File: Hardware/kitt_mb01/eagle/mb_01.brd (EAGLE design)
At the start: 160 x 100 mm, 120 parts, among them IC2.00 BQ24266RGET, IC3.01 LSM9DS1, U1.01 RT8293A, U6.01 TPS61032RSARPSDO-G16, U7.01 SI1922EDH, U7.03 SI1922EDH, U7.2 SI1922EDH, X2.01 S2B-PH-K-S(LF)(SN), X7.02 ARDUINO_UNO, X7.03 CON_HEADER_1X02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

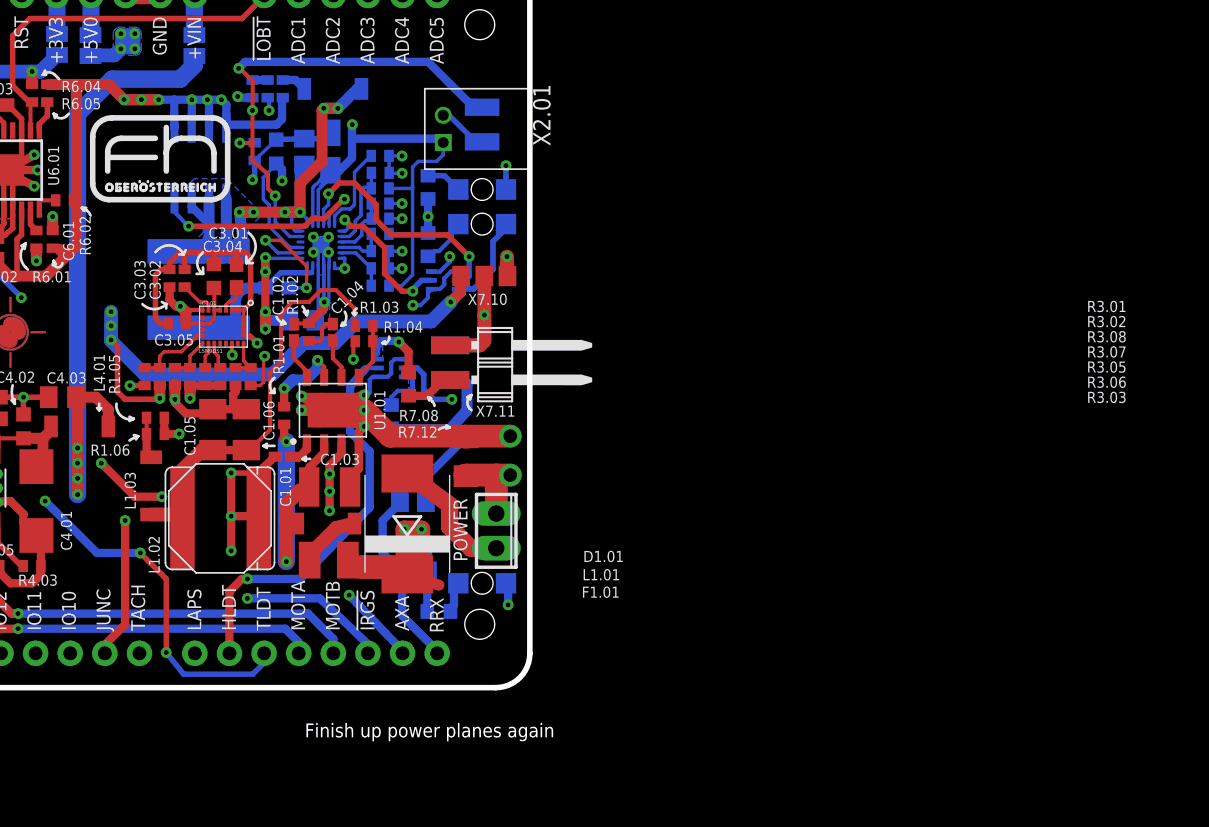
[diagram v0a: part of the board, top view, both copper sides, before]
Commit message: snapshot of mb01 board layout : finishing touches edition -> finished all placement, signal routing and component label silkscreen -> next up is maximization of power routes at layer 2 and -> ground pours on top and bottom with sufficient ground stitching
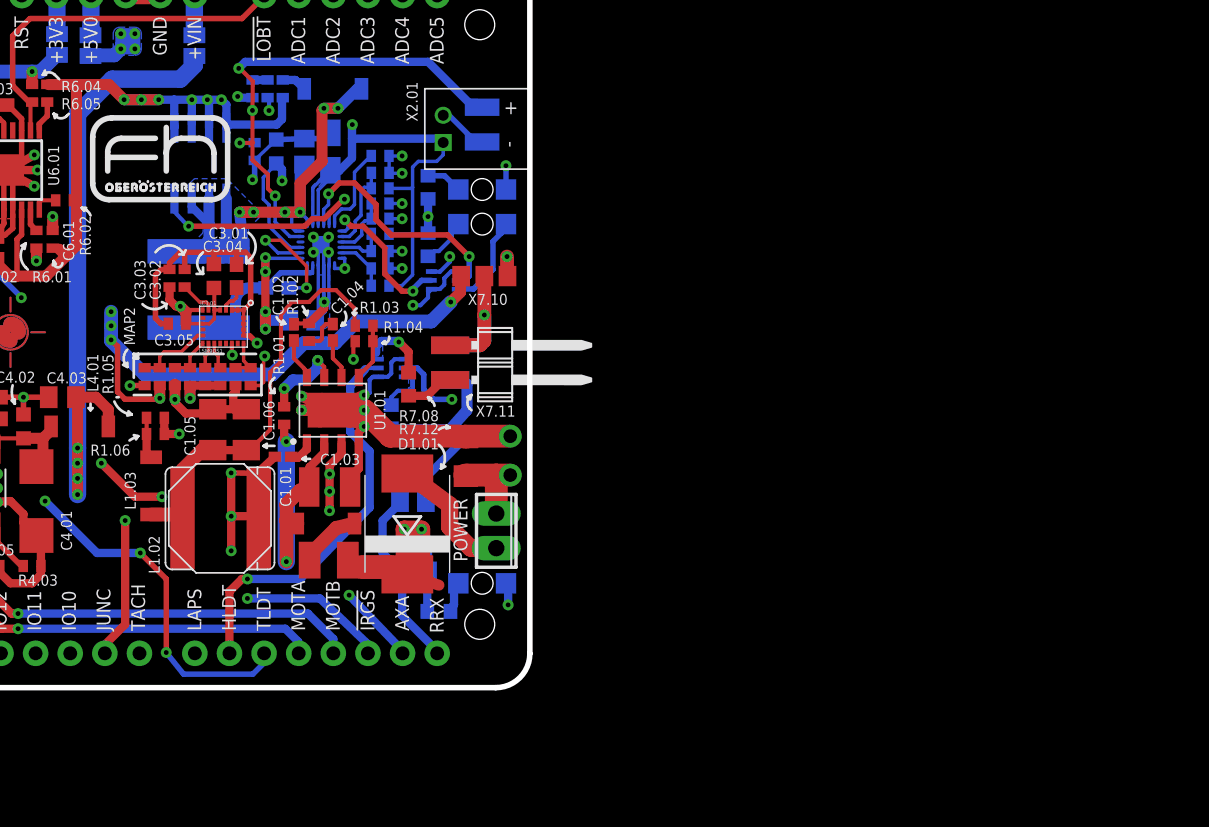
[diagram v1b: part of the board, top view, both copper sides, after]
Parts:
- renumbered IC2.00 to IC2.0, R7,01 to R7.16, R7,02 to R7.13, R7,04 to R7.14, R7,05 to R7.15
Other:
- board text added: "EXT.NTC"
- board text added: "MAP1"
- board text added: "MAP2"
- board text added: "TOP"
- board text removed: "<-- Rail Power Leads"
- board text removed: "EXT.PTC"
- board text removed: "Finish up power planes again"
- board text removed: "Motor Leads -->"
- board text removed: "SPEEDBOARD --> LAPDETECTOR -->"

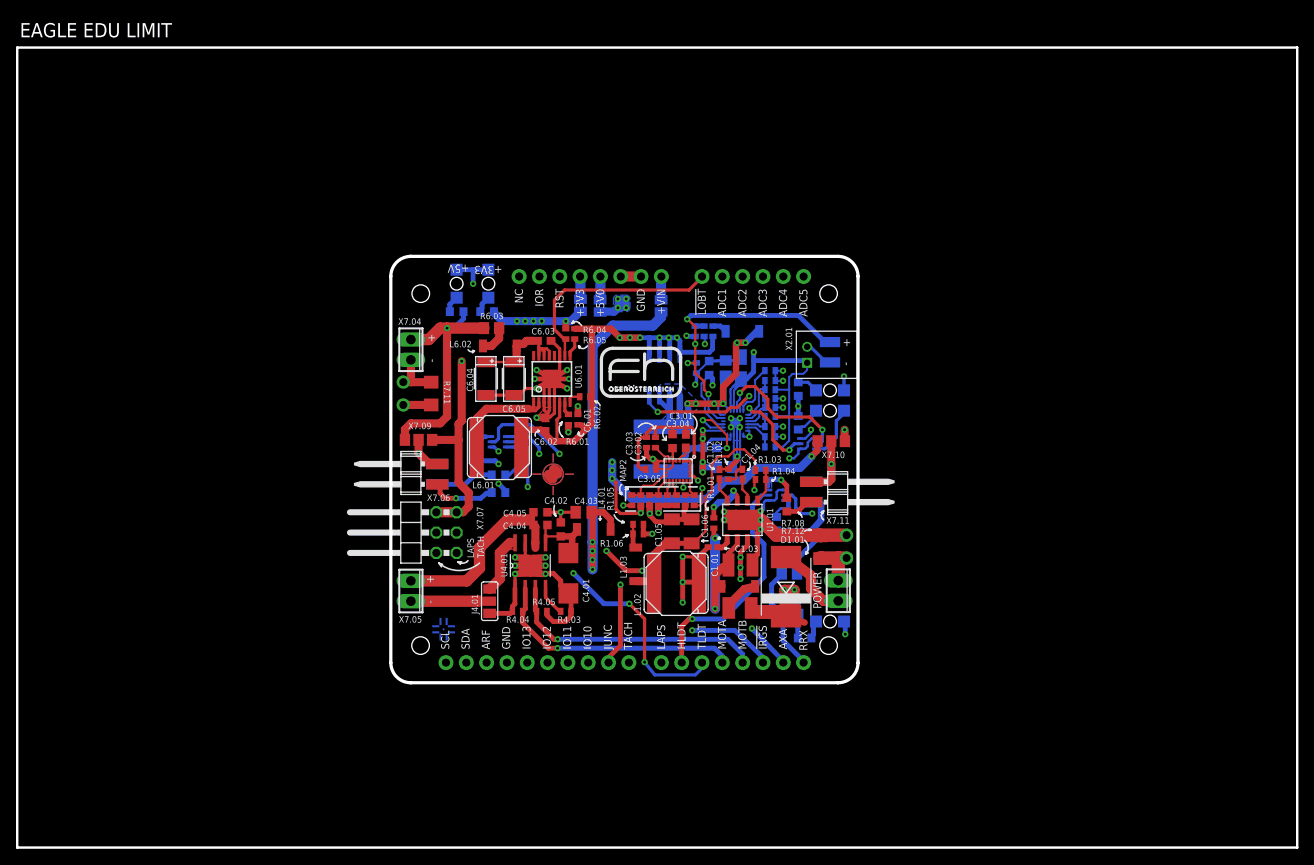
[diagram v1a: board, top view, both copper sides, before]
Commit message: snapshot of mb01 board layout -> where is the 3V3 supply again? -> there is none. will add optional LDO regulator which is on the BOM
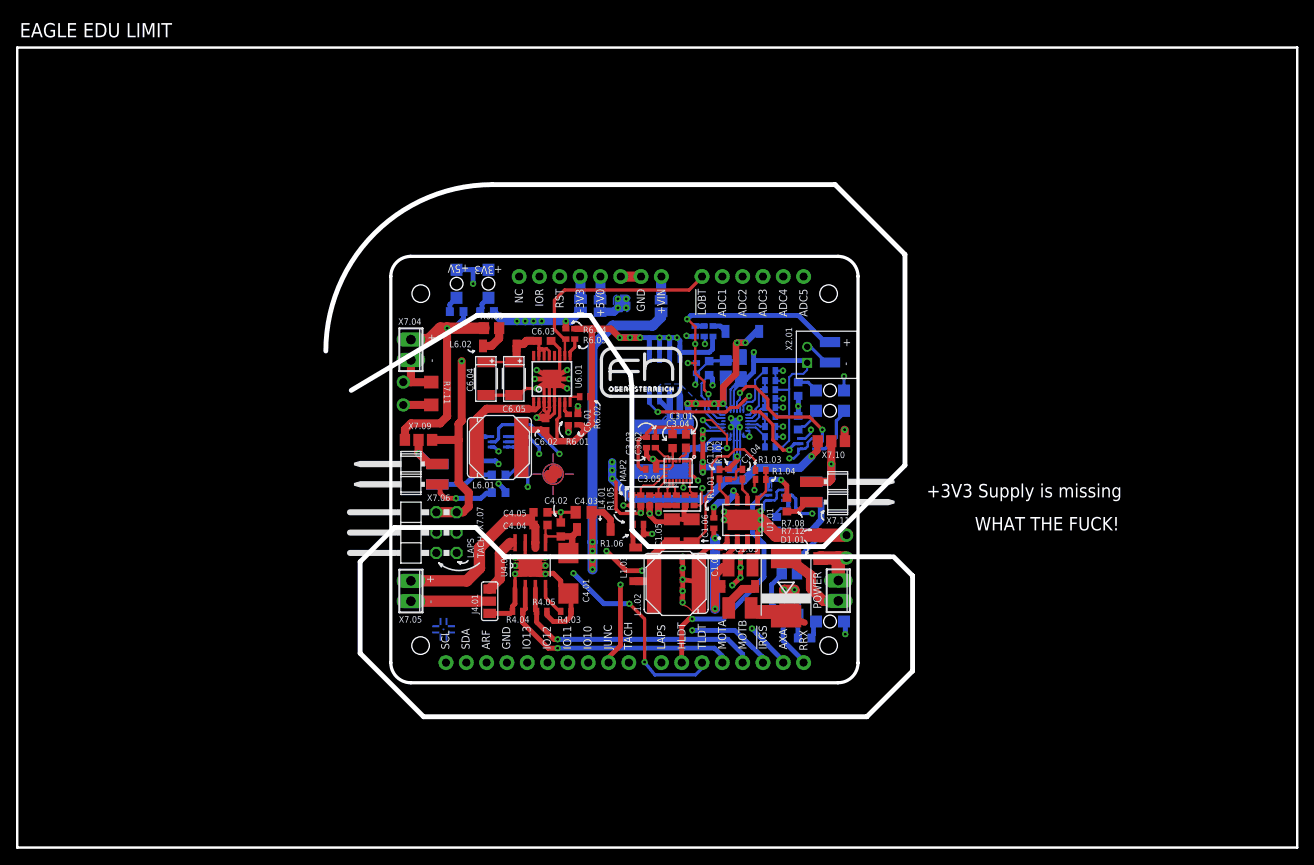
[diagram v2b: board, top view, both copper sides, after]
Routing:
- net N$88: track 17.5 -> 18.7 mm, vias 6 -> 9
- added copper zone on layer 1, net N$88
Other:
- outline, holes or cut-outs redrawn
- board text added: "+3V3 Supply is missing"
- board text added: "WHAT THE FUCK!"
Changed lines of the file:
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@@
 <setting verticaltext="up"/>
 </settings>
-<grid distance="3.125" unitdist="mil" unit="mil" style="lines" multiple="1" display="yes" altdistance="0.0125" altunitdist="inch" altunit="inch"/>
+<grid distance="6.25" unitdist="mil" unit="mil" style="lines" multiple="1" display="yes" altdistance="0.0125" altunitdist="inch" altunit="inch"/>
 <layers>
 <layer number="1" name="Top" color="4" fill="1" visible="yes" active="yes"/>
-<layer number="2" name="Route2" color="29" fill="0" visible="yes" active="yes"/>
+<layer number="2" name="Route2" color="29" fill="0" visible="no" active="yes"/>
 <layer number="3" name="Route3" color="24" fill="9" visible="yes" active="yes"/>
 <layer number="14" name="Route14" color="1" fill="6" visible="no" active="no"/>
@@
 <text x="91.1225" y="29.845" size="0.6096" layer="26" font="vector" ratio="13" rot="MR0" align="center-left">TOP</text>
 <text x="90.96375" y="32.623125" size="0.6096" layer="26" font="vector" ratio="13" rot="MR0" align="center-left">TOP</text>
+<wire x1="41.75125" y1="57.15" x2="57.4675" y2="66.51625" width="0.6096" layer="46"/>
+<wire x1="57.4675" y1="66.51625" x2="71.59625" y2="66.51625" width="0.6096" layer="46"/>
+<wire x1="71.59625" y1="66.51625" x2="76.67625" y2="59.055" width="0.6096" layer="46"/>
+<wire x1="76.67625" y1="59.055" x2="76.835" y2="57.4675" width="0.6096" layer="46"/>
+<wire x1="76.835" y1="57.4675" x2="76.835" y2="39.6875" width="0.6096" layer="46"/>
+<wire x1="76.835" y1="39.6875" x2="78.89875" y2="37.62375" width="0.6096" layer="46"/>
+<wire x1="78.89875" y1="37.62375" x2="100.80625" y2="37.62375" width="0.6096" layer="46"/>
+<wire x1="100.80625" y1="37.62375" x2="110.96625" y2="47.78375" width="0.6096" layer="46"/>
+<wire x1="110.96625" y1="47.78375" x2="110.96625" y2="74.13625" width="0.6096" layer="46"/>
+<wire x1="110.96625" y1="74.13625" x2="102.235" y2="82.8675" width="0.6096" layer="46"/>
+<wire x1="102.235" y1="82.8675" x2="59.3725" y2="82.8675" width="0.6096" layer="46"/>
+<wire x1="59.3725" y1="82.8675" x2="38.57625" y2="62.07125" width="0.6096" layer="46" curve="90"/>
+<wire x1="109.22" y1="36.35375" x2="60.96" y2="36.35375" width="0.6096" layer="46"/>
+<wire x1="60.96" y1="36.35375" x2="57.30875" y2="40.005" width="0.6096" layer="46"/>
+<wire x1="57.30875" y1="40.005" x2="47.14875" y2="40.005" width="0.6096" layer="46"/>
+<wire x1="47.14875" y1="40.005" x2="42.8625" y2="35.71875" width="0.6096" layer="46"/>
+<wire x1="42.8625" y1="35.71875" x2="42.8625" y2="24.28875" width="0.6096" layer="46"/>
+<wire x1="42.8625" y1="24.28875" x2="50.8" y2="16.35125" width="0.6096" layer="46"/>
+<wire x1="50.8" y1="16.35125" x2="106.20375" y2="16.35125" width="0.6096" layer="46"/>
+<wire x1="106.20375" y1="16.35125" x2="111.91875" y2="22.06625" width="0.6096" layer="46"/>
+<wire x1="111.91875" y1="22.06625" x2="111.91875" y2="33.9725" width="0.6096" layer="46"/>
+<wire x1="111.91875" y1="33.9725" x2="109.5375" y2="36.35375" width="0.6096" layer="46"/>
+<text x="113.665" y="44.60875" size="1.6764" layer="46" font="vector" ratio="13" align="center-left">+3V3 Supply is missing</text>
+<text x="119.6975" y="40.48125" size="1.6764" layer="46" font="vector" ratio="13" align="center-left">WHAT THE FUCK!</text>
 </plain>
 <attributes>
@@
 <contactref element="F1.01" pad="2"/>
 <contactref element="L1.01" pad="1"/>
-<wire x1="92.23845" y1="32.641225" x2="90.902475" y2="32.323725" width="1.016" layer="1"/>
-<wire x1="90.902475" y1="32.323725" x2="88.946025" y2="30.367275" width="1.016" layer="1"/>
-<wire x1="88.946025" y1="30.367275" x2="88.946025" y2="29.95275" width="1.016" layer="1"/>
+<wire x1="90.66435" y1="32.323725" x2="88.946025" y2="30.6054" width="1.016" layer="1"/>
+<wire x1="88.946025" y1="30.6054" x2="88.946025" y2="29.95275" width="1.016" layer="1"/>
+<wire x1="90.66435" y1="32.323725" x2="91.92095" y2="32.323725" width="1.016" layer="1"/>
+<wire x1="91.92095" y1="32.323725" x2="92.23845" y2="32.641225" width="1.016" layer="1"/>
 </signal>
 <signal name="N$81">
@@
 <wire x1="85.4075" y1="33.18" x2="85.09" y2="33.02" width="0.3048" layer="1"/>
 <wire x1="85.09" y1="33.02" x2="85.213125" y2="33.02" width="0.3048" layer="1"/>
-<via x="90.40125" y="33.580625" extent="1-16" drill="0.35" diameter="0.6"/>
+<via x="90.40125" y="33.739375" extent="1-16" drill="0.35" diameter="0.6"/>
 <via x="83.185" y="36.35375" extent="1-16" drill="0.35" diameter="0.6"/>
-<via x="83.185" y="33.17875" extent="1-16" drill="0.35" diameter="0.6"/>
-<wire x1="83.185" y1="33.17875" x2="83.185" y2="36.35375" width="0.6096" layer="1"/>
-<wire x1="83.185" y1="30.63875" x2="83.185" y2="33.17875" width="0.6096" layer="1"/>
-<wire x1="83.185" y1="33.17875" x2="85.4075" y2="33.18" width="0.6096" layer="1"/>
+<via x="83.185" y="33.49625" extent="1-16" drill="0.35" diameter="0.6"/>
+<wire x1="83.185" y1="33.49625" x2="83.185" y2="34.925" width="0.6096" layer="1"/>
+<wire x1="83.185" y1="34.925" x2="83.185" y2="36.35375" width="0.6096" layer="1"/>
+<wire x1="83.185" y1="30.63875" x2="83.185" y2="32.0675" width="0.6096" layer="1"/>
+<wire x1="83.185" y1="32.0675" x2="83.185" y2="33.49625" width="0.6096" layer="1"/>
+<wire x1="83.185" y1="33.49625" x2="85.4075" y2="33.18" width="0.6096" layer="1"/>
 <polygon width="1.016" layer="3" thermals="no">
 <vertex x="83.185" y="36.35375"/>
 <vertex x="83.185" y="30.63875" curve="45.11449"/>
 <vertex x="89.614375" y="32.623125" curve="52.900997"/>
-<vertex x="90.96375" y="34.210625"/>
-<vertex x="91.360625" y="37.226875"/>
-<vertex x="90.408125" y="37.226875" curve="27.460472"/>
-<vertex x="89.535" y="36.83" curve="-18.924644"/>
-<vertex x="85.963125" y="36.35375"/>
+<vertex x="90.4875" y="33.575625"/>
+<vertex x="90.64625" y="36.274375" curve="90"/>
+<vertex x="90.249375" y="36.433125" curve="-18.924644"/>
 </polygon>
 <wire x1="83.185" y1="36.35375" x2="85.09" y2="36.33" width="0.4064" layer="1"/>
@@
 <wire x1="86.395" y1="37.544375" x2="86.36" y2="37.509375" width="0.6096" layer="1"/>
 <wire x1="86.36" y1="37.509375" x2="85.09" y2="36.33" width="0.6096" layer="1"/>
-<wire x1="90.40125" y1="33.580625" x2="90.40125" y2="33.806875" width="0.6096" layer="1"/>
+<wire x1="90.40125" y1="33.739375" x2="90.40125" y2="33.806875" width="0.6096" layer="1"/>
 <wire x1="90.40125" y1="33.806875" x2="90.408125" y2="33.81375" width="0.6096" layer="1"/>
 <via x="83.185" y="30.63875" extent="1-16" drill="0.35"/>
@@
 <wire x1="90.408125" y1="36.909375" x2="91.28125" y2="37.7825" width="0.6096" layer="1"/>
 <wire x1="91.28125" y1="37.7825" x2="91.28125" y2="38.5575" width="0.6096" layer="1"/>
+<wire x1="90.408125" y1="33.734375" x2="89.37625" y2="32.781875" width="0.6096" layer="1"/>
+<via x="89.37625" y="32.781875" extent="1-16" drill="0.35"/>
+<via x="83.185" y="34.925" extent="1-16" drill="0.35"/>
+<via x="83.185" y="32.0675" extent="1-16" drill="0.35"/>
+<polygon width="0.6096" layer="1" thermals="no">
+<vertex x="82.8675" y="36.195"/>
+<vertex x="82.8675" y="30.63875" curve="93.096691"/>
+<vertex x="83.185" y="30.32125" curve="-44.209773"/>
+<vertex x="84.29625" y="29.5783"/>
+<vertex x="85.725" y="29.581475"/>
+<vertex x="85.725" y="36.5125"/>
+<vertex x="83.185" y="36.67125" curve="90"/>
+</polygon>
 </signal>
 <signal name="N$89">
@@
 <wire x1="91.836875" y1="27.384375" x2="88.9" y2="28.41625" width="0.6096" layer="3" curve="90"/>
 <wire x1="88.9" y1="28.41625" x2="85.328125" y2="28.971875" width="0.6096" layer="3" curve="-87.617023"/>
-<wire x1="85.328125" y1="28.971875" x2="83.34375" y2="28.8925" width="0.6096" layer="3" curve="126.40107"/>
-<wire x1="83.34375" y1="28.8925" x2="82.470625" y2="28.495625" width="0.6096" layer="3" curve="-57.383905"/>
+<wire x1="85.328125" y1="28.971875" x2="83.5025" y2="28.8925" width="0.6096" layer="3" curve="126.40107"/>
+<wire x1="83.5025" y1="28.8925" x2="82.470625" y2="28.495625" width="0.6096" layer="3" curve="-57.383905"/>
 <wire x1="82.470625" y1="28.495625" x2="79.21625" y2="32.54375" width="0.6096" layer="3" curve="-92.108595"/>
 <wire x1="79.21625" y1="32.54375" x2="78.105" y2="34.6075" width="0.6096" layer="3" curve="75.990386"/>

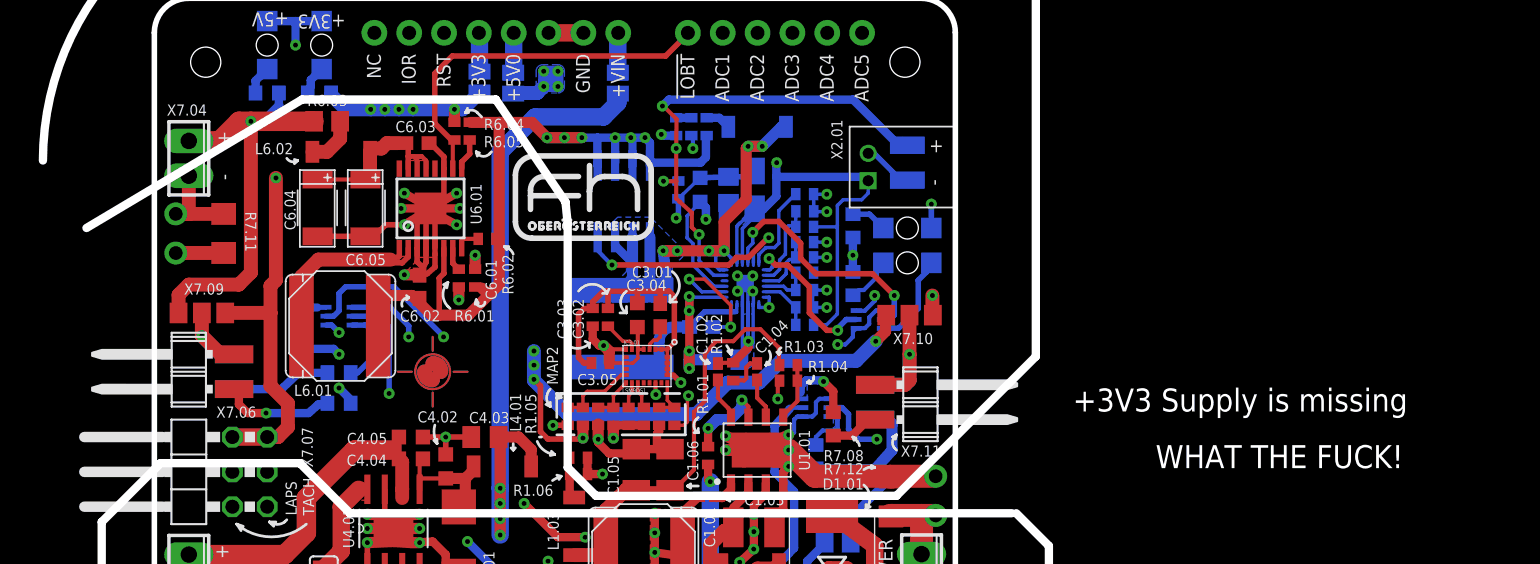
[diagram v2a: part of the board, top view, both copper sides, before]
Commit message: snapshot of mb01 board layout -> added 3V3 LDO regulator (neither ideal in placement nor routing, but w/e)
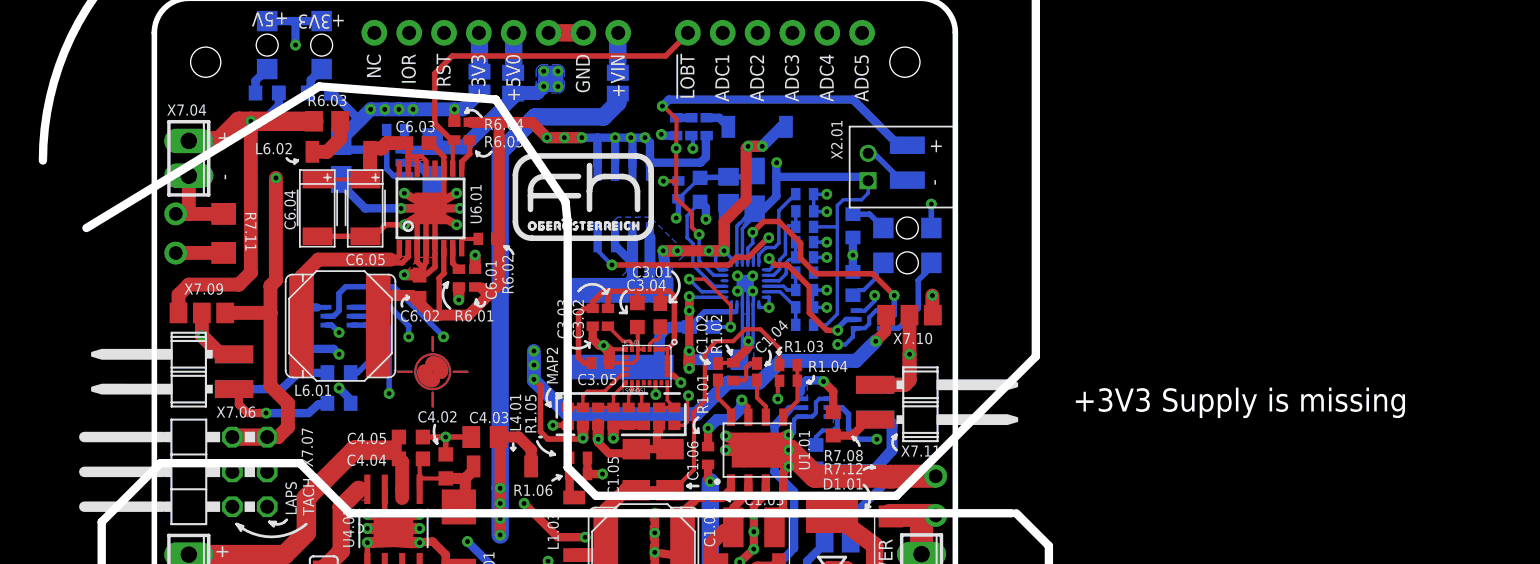
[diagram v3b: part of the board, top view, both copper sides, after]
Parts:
- added C1.07, C1.08: 1uF, rcl:A/3216-18R
- added R1.07: [0R], rcl:R0402
- added U1: MIC5205-3.3YM5TR, kitt.ic:SOT95P280X130-5N
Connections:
- new net N$49: R1.07.1, U1.3
- net +3V3: now also C1.08.+, U1.5
- net +5V: now also C1.07.+, R1.07.2, U1.1
- net GND: now also C1.07.-, C1.08.-, U1.2
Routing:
- net +5V: track 151.3 -> 163.5 mm
- net GND: track 245.8 -> 257.9 mm
- net +3V3: track 160.7 -> 166.0 mm
- net N$49: track 0.00 -> 4.34 mm
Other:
- outline, holes or cut-outs redrawn
- board text removed: "WHAT THE FUCK!"
